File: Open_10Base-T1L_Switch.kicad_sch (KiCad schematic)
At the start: 0 parts

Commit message: Update Schematic Name
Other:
- sheet PoDL REG2 renamed PoDL REG1
- sheet PoDL REG1: file PoDL_REG2.kicad_sch -> PoDL_REG1.kicad_sch
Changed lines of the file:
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@@
     (stroke (width 0.1524) (type solid) (color 0 0 0 0))
     (fill (color 0 0 0 0.0000))
-    (property "Sheet name" "PoDL REG2" (id 0) (at 111.76 152.9584 0)
+    (property "Sheet name" "PoDL REG1" (id 0) (at 111.76 152.9584 0)
       (effects (font (size 1.27 1.27)) (justify left bottom))
     )
-    (property "Sheet file" "PoDL_REG2.kicad_sch" (id 1) (at 111.76 172.0346 0)
+    (property "Sheet file" "PoDL_REG1.kicad_sch" (id 1) (at 111.76 172.0346 0)
       (effects (font (size 1.27 1.27)) (justify left top))
     )

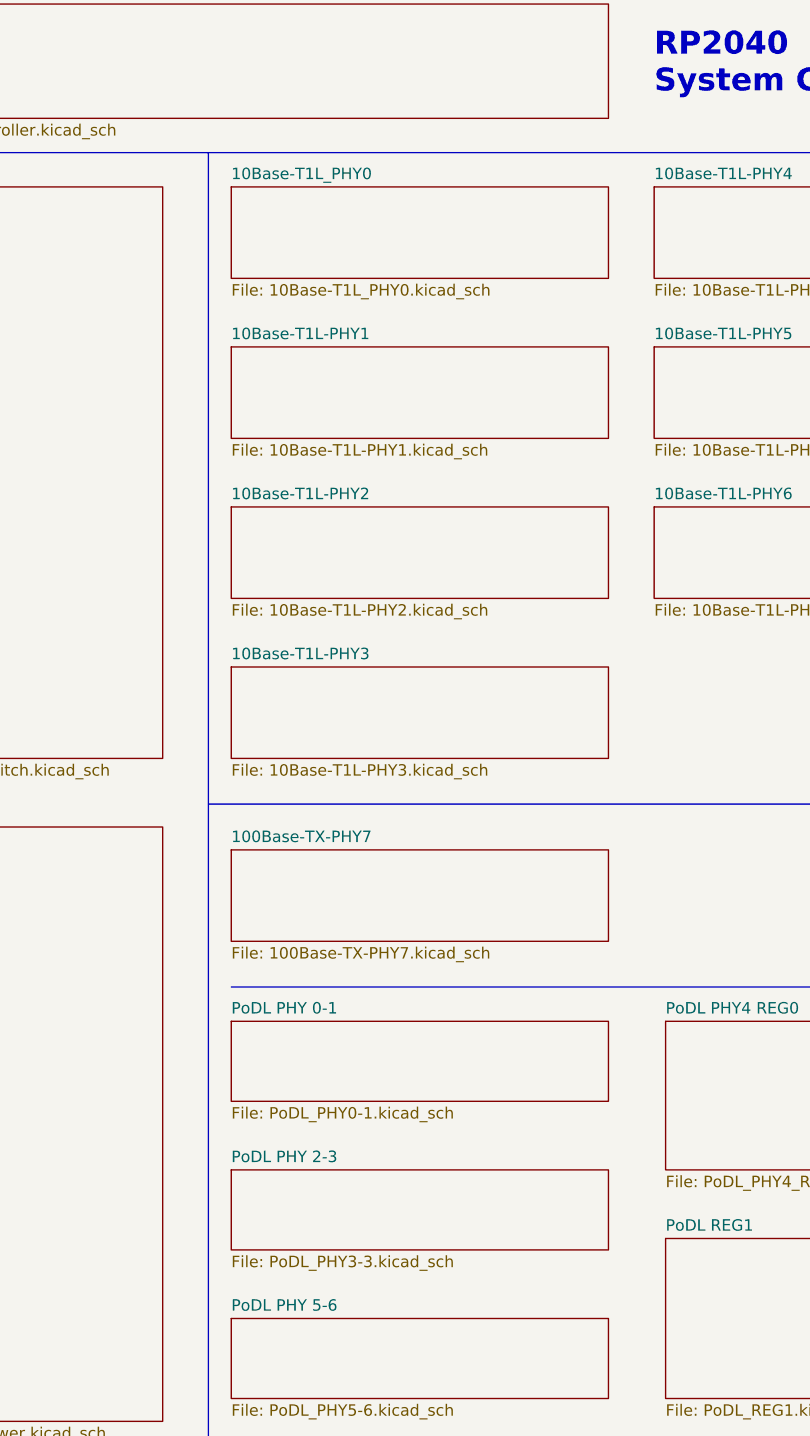
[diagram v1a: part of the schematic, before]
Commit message: Renaming Sheets
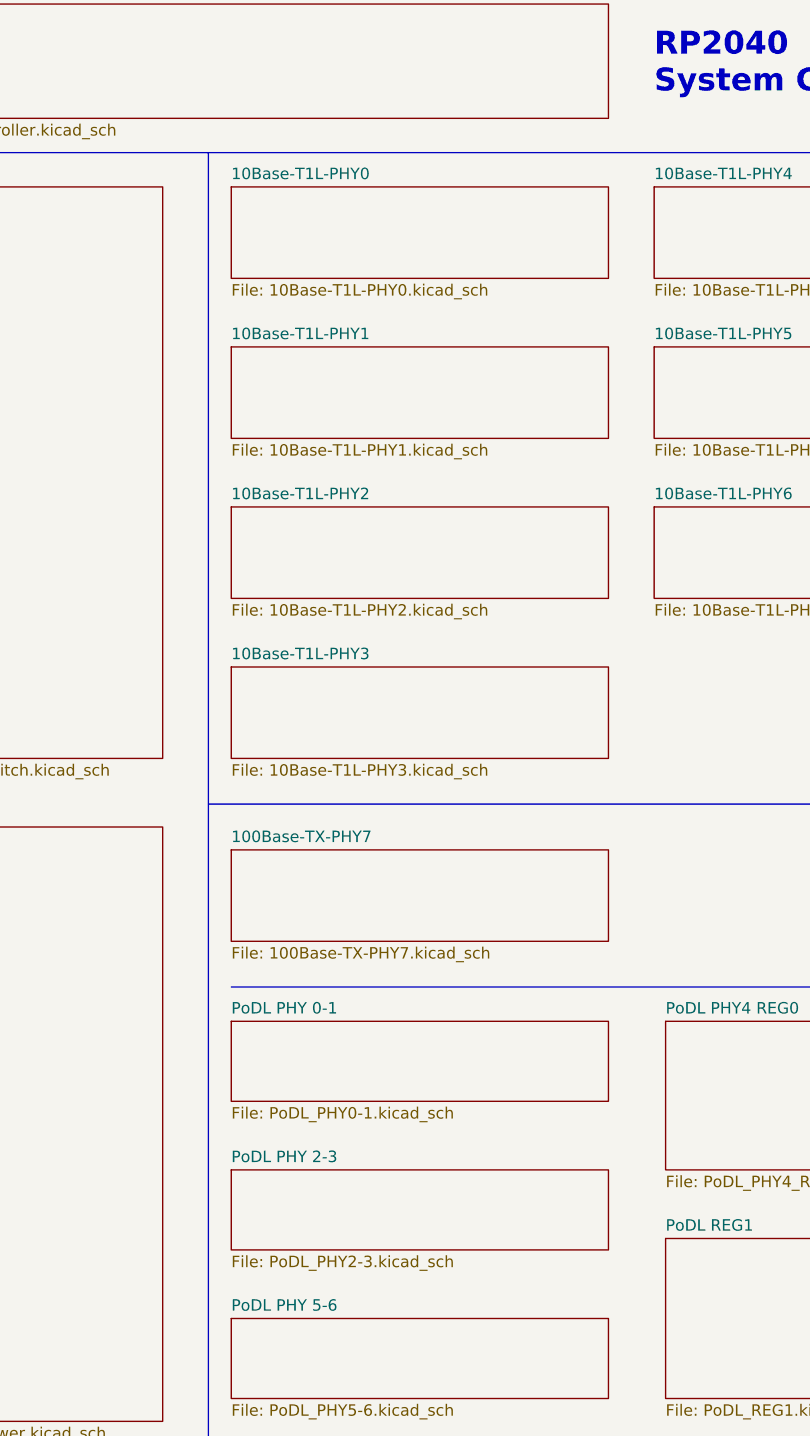
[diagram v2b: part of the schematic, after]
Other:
- sheet 10Base-T1L_PHY0 renamed 10Base-T1L-PHY0
- sheet 10Base-T1L-PHY0: file 10Base-T1L_PHY0.kicad_sch -> 10Base-T1L-PHY0.kicad_sch
- sheet PoDL PHY 2-3: file PoDL_PHY3-3.kicad_sch -> PoDL_PHY2-3.kicad_sch
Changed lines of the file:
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@@
     (stroke (width 0.1524) (type solid) (color 0 0 0 0))
     (fill (color 0 0 0 0.0000))
-    (property "Sheet name" "10Base-T1L_PHY0" (id 0) (at 63.5 36.1184 0)
+    (property "Sheet name" "10Base-T1L-PHY0" (id 0) (at 63.5 36.1184 0)
       (effects (font (size 1.27 1.27)) (justify left bottom))
     )
-    (property "Sheet file" "10Base-T1L_PHY0.kicad_sch" (id 1) (at 63.5 47.5746 0)
+    (property "Sheet file" "10Base-T1L-PHY0.kicad_sch" (id 1) (at 63.5 47.5746 0)
       (effects (font (size 1.27 1.27)) (justify left top))
     )
@@
       (effects (font (size 1.27 1.27)) (justify left bottom))
     )
-    (property "Sheet file" "PoDL_PHY3-3.kicad_sch" (id 1) (at 63.5 155.5246 0)
+    (property "Sheet file" "PoDL_PHY2-3.kicad_sch" (id 1) (at 63.5 155.5246 0)
       (effects (font (size 1.27 1.27)) (justify left top))
     )
